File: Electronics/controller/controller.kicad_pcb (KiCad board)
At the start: 2 copper layers, 99.1 x 56.5 mm, 31 parts, among them P1 POWER, P2 PANEL_1, P3 PANEL_2, Q1 P55NF, SW1 SW_PUSH, U1 LM7805CT, U2 74HC595, U3 Arduino_Pro_Micro

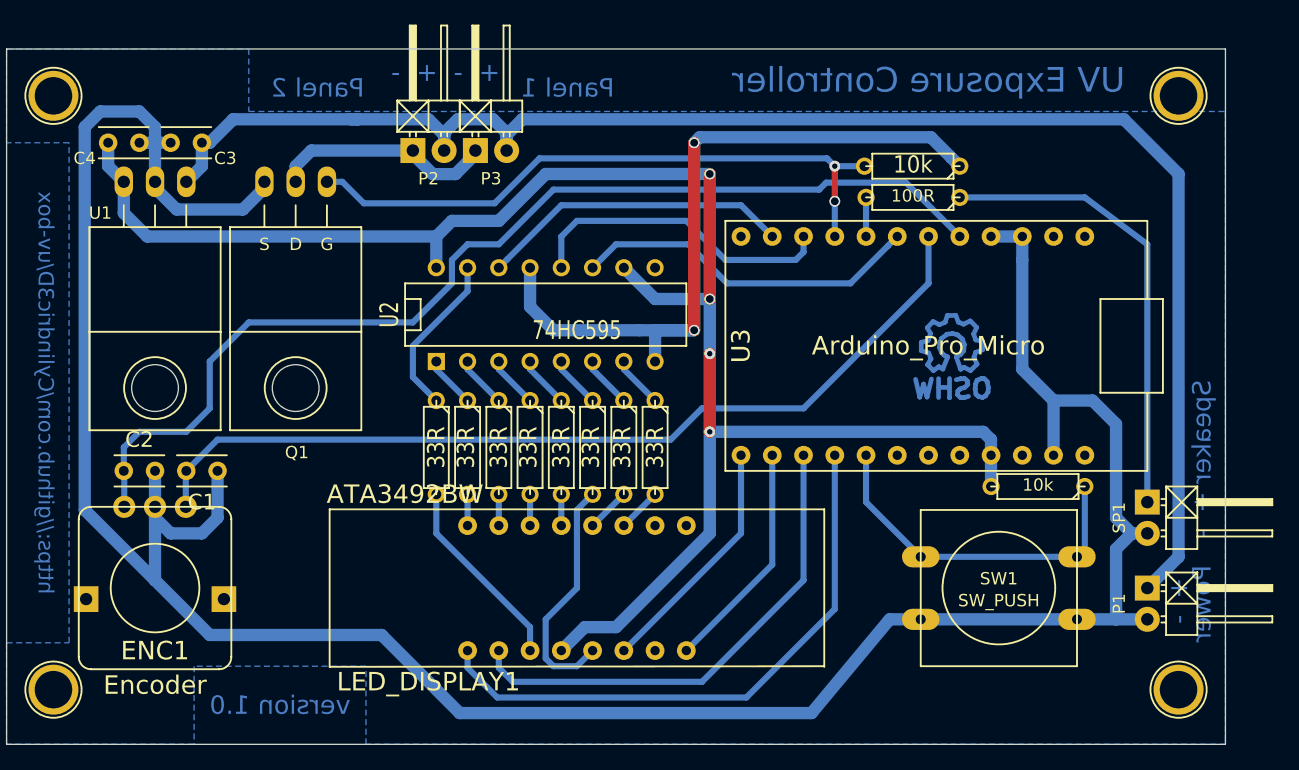
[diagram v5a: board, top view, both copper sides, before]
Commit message: Made board more home-brew friendly.
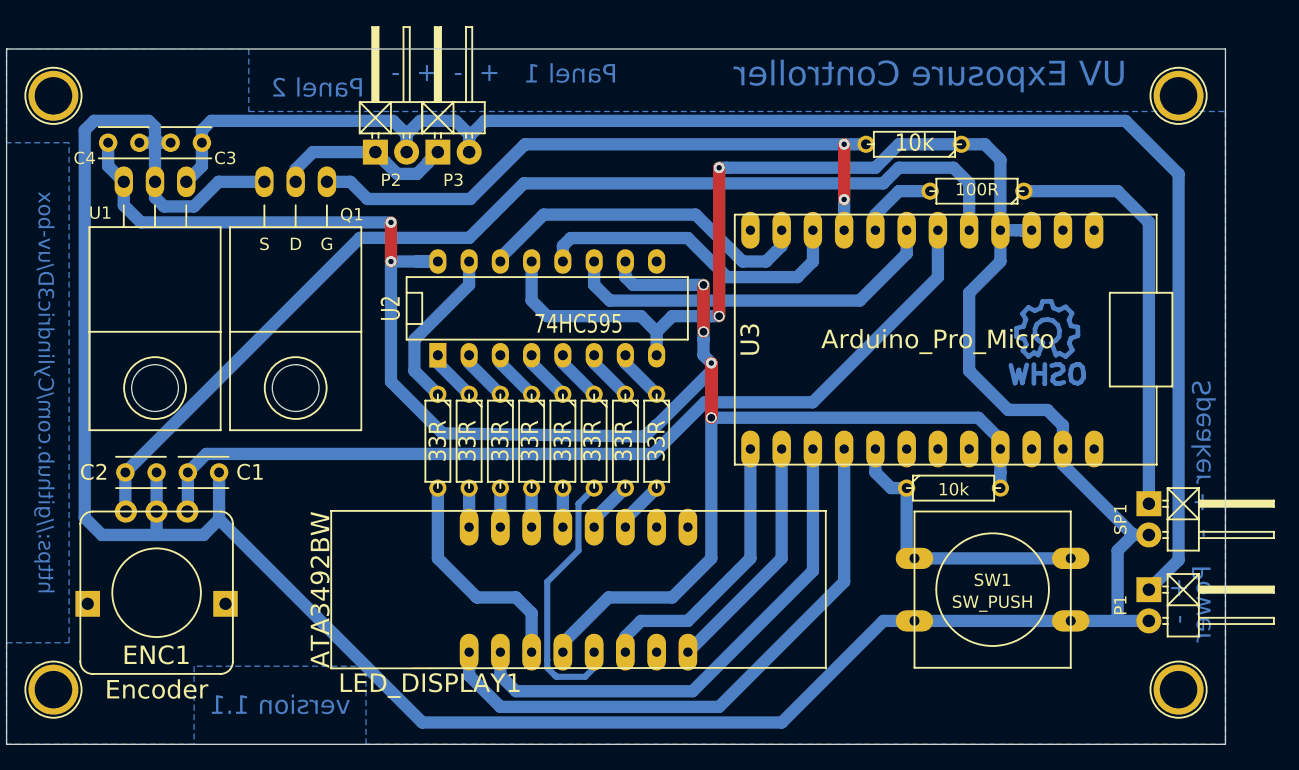
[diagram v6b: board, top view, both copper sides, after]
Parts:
- moved Symbol_OSHW-Logo_CopperTop 7.83 mm to (133.3, 38.7)
- moved R2 6.86 mm to (125.7, 51.4), turned to 0 degrees
- moved R12 5.23 mm to (127.6, 27.3)
- moved P2 3.05 mm to (80.0, 24.1)
- moved P3 3.05 mm to (85.1, 24.1)
- moved R4 1.78 mm to (122.6, 23.5)
- moved U3 0.92 mm to (132.1, 40.6)
- moved SW1 0.52 mm to (128.9, 59.7)
- moved R11 0.52 mm to (88.9, 47.6)
- moved R7 0.52 mm to (94.0, 47.6)
- moved R1 0.52 mm to (99.1, 47.6)
- moved R10 0.52 mm to (101.6, 47.6)
- moved R5 0.52 mm to (91.4, 47.6)
- moved R6 0.52 mm to (86.4, 47.6)
- moved R8 0.52 mm to (83.8, 47.6)
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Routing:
- net VCC: track 140.0 -> 155.8 mm, vias 4 -> 6
- net GND: track 279.1 -> 271.1 mm
- net /D18: track 28.8 -> 24.7 mm
- net /12VGND: track 18.5 -> 14.8 mm
- net Net-(R12-Pad1): track 37.5 -> 34.1 mm
- net /PWM5: track 3.18 -> 6.50 mm
- net /D10: track 19.8 -> 23.0 mm
- net /D4: track 28.4 -> 31.3 mm
- net /D8: track 25.4 -> 28.0 mm
- net Net-(LED_DISPLAY1-Pad3): track 15.9 -> 18.4 mm
- net Net-(LED_DISPLAY1-Pad5): track 19.5 -> 21.9 mm
- net /D14: track 40.2 -> 41.8 mm
- net /D3: track 73.4 -> 74.9 mm
- net +12V: track 128.4 -> 127.0 mm
- net /D6: track 52.1 -> 53.2 mm
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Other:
- board text added: "version 1.1"
- board text removed: "version 1.0"

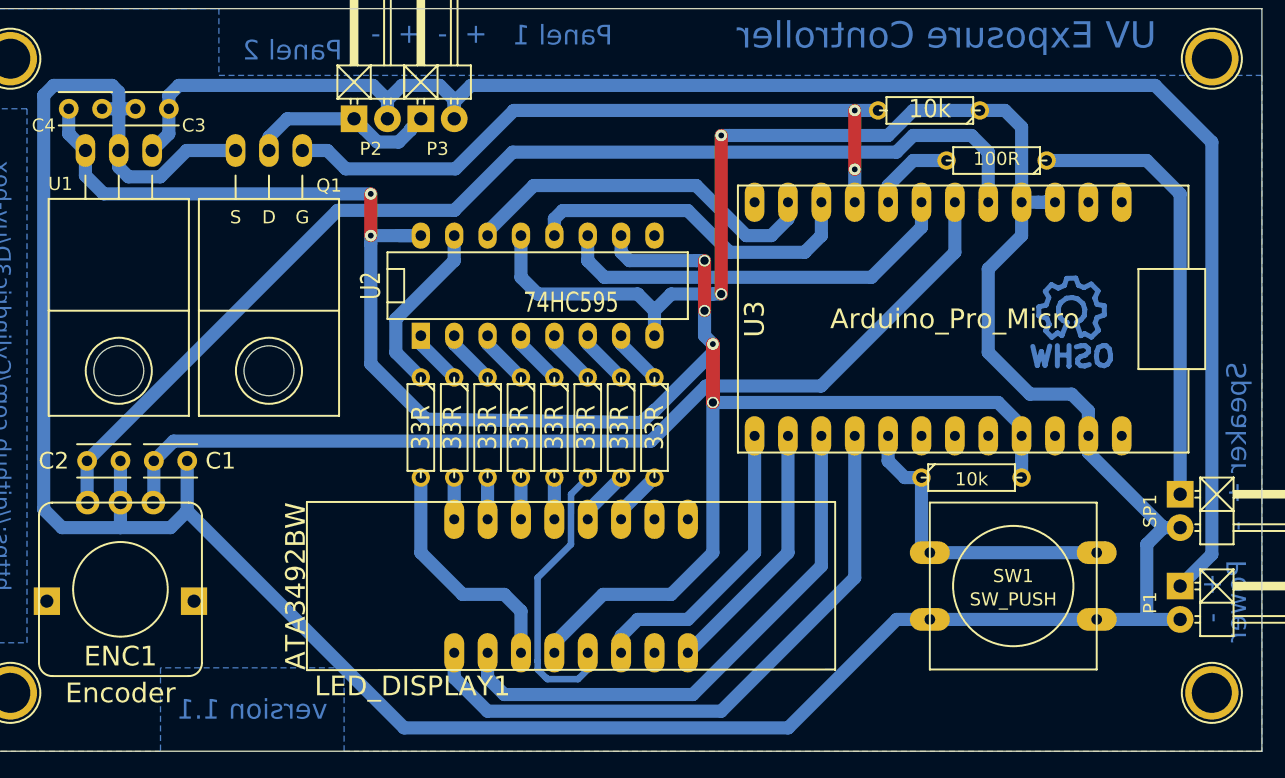
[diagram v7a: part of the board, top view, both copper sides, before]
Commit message: Fixes based on first real build.
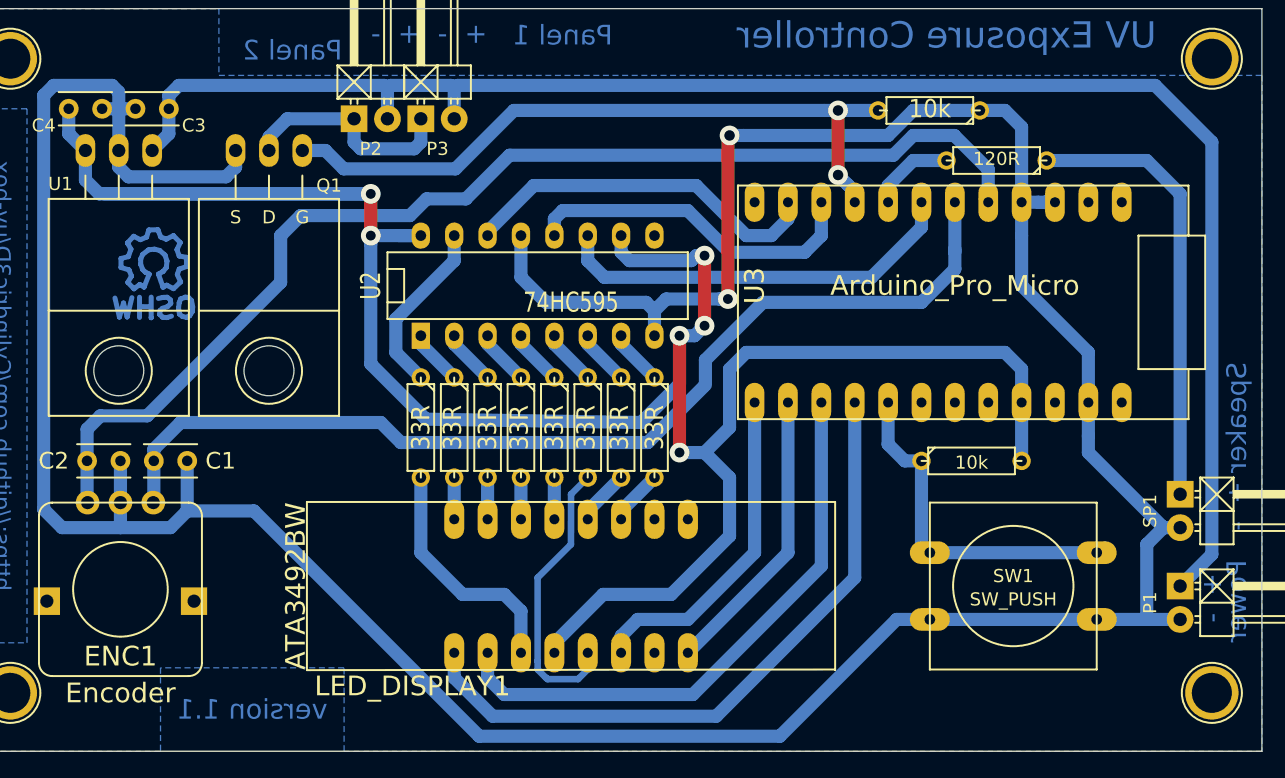
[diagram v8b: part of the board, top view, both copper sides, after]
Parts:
- R12: value 100R -> 120R
- moved Symbol_OSHW-Logo_CopperTop 69.9 mm to (63.5, 35.1)
- moved U3 2.54 mm to (132.1, 38.1)
- moved R2 1.27 mm to (125.7, 50.2)
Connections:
- R1 pad 1: /E -> /COL
- R7 pad 1: /COL -> /C
- R9 pad 1: /C -> /E
- U2 pad 4: /COL -> /C
- U2 pad 5: /C -> /E
- U2 pad 6: /E -> /COL
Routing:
- net VCC: track 155.8 -> 185.6 mm
- net /D3: track 74.9 -> 78.7 mm
- net /D15: track 48.4 -> 51.3 mm
- net /D2: track 86.7 -> 89.4 mm
- net GND: track 271.1 -> 268.5 mm
- net /D18: track 24.7 -> 27.3 mm
- net /D16: track 19.7 -> 22.2 mm
- net /D14: track 41.8 -> 44.3 mm
- net /D10: track 23.0 -> 25.5 mm
- net /12VGND: track 14.8 -> 17.3 mm
- net +12V: track 127.0 -> 126.0 mm
- net /D6: track 53.2 -> 53.7 mm
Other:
- net class Default: via_dia 0.889 -> 1.5; via_drill 0.635 -> 0.8
- net class Power: via_dia 0.889 -> 1.5; via_drill 0.635 -> 0.8
